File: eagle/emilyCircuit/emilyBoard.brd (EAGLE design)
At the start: 73.3 x 47 mm, 12 parts

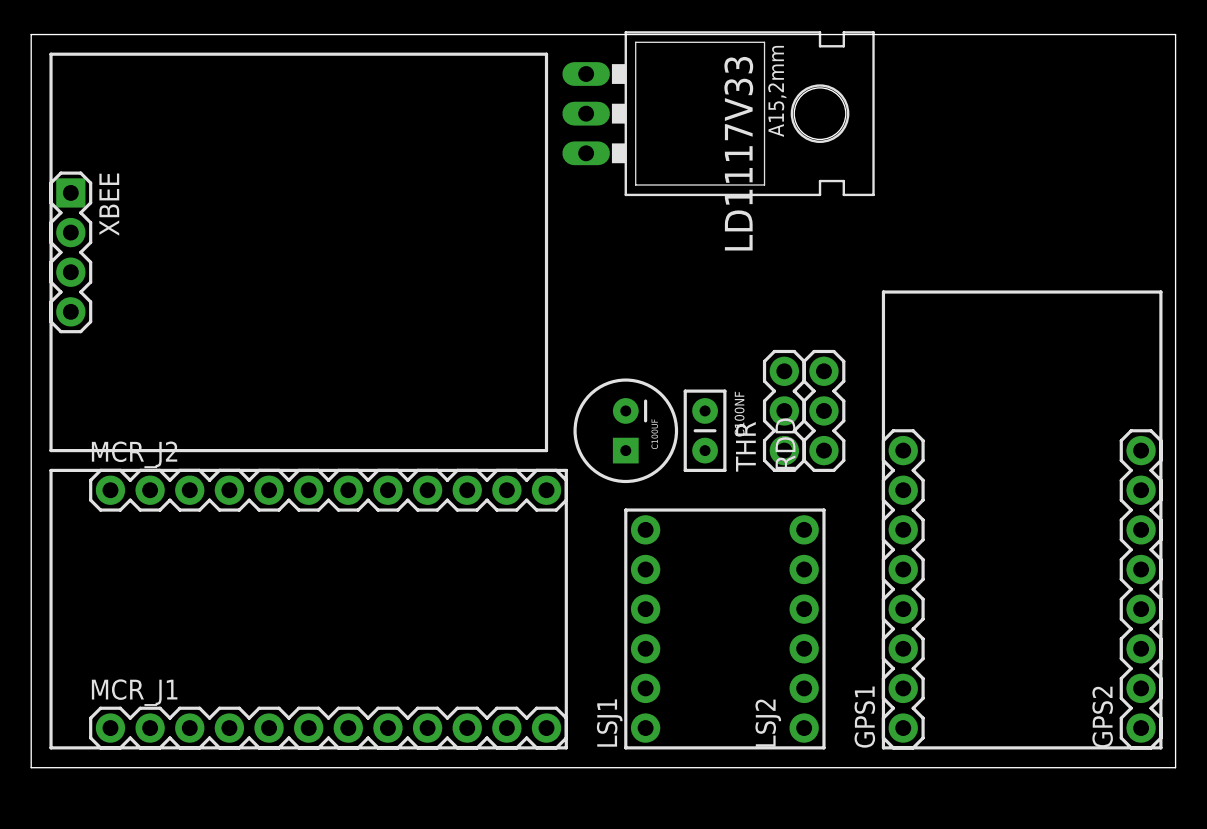
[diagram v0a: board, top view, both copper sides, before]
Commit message: Added connections to emily board
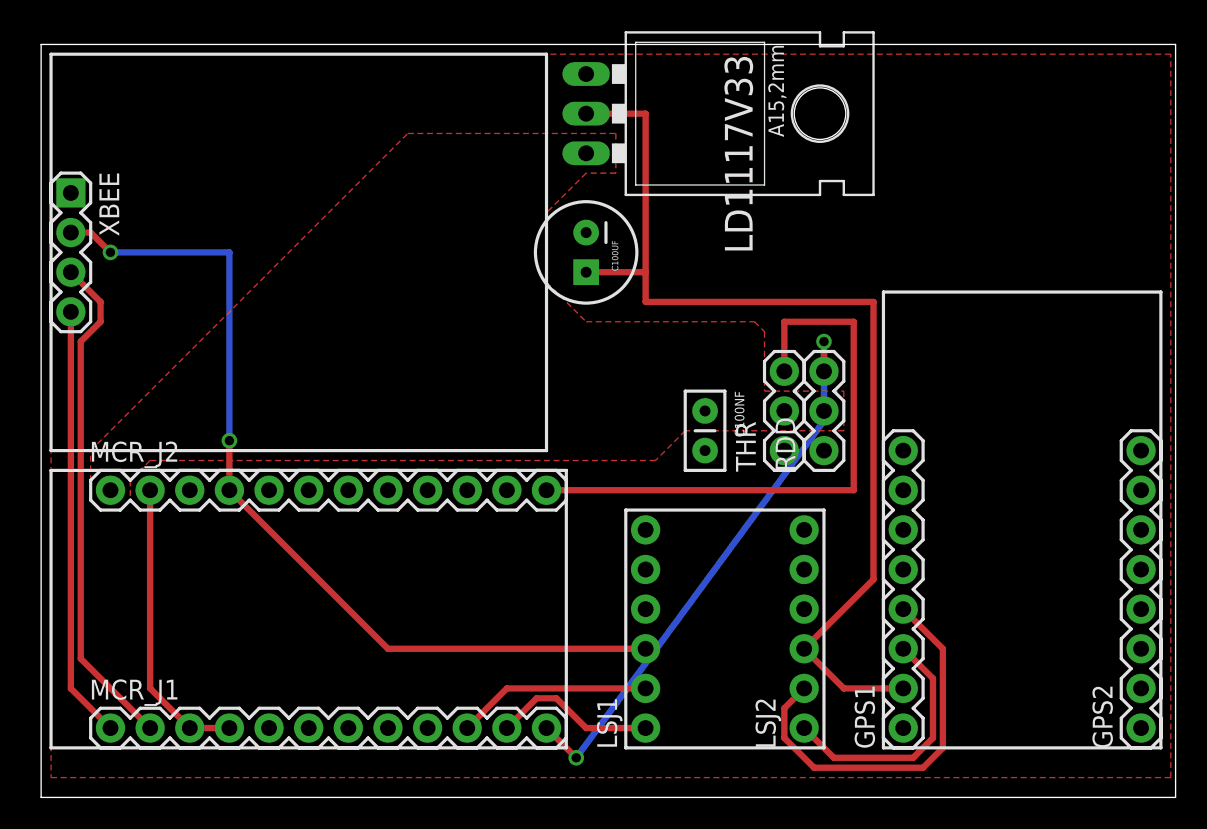
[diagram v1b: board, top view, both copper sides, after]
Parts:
- moved C100UF 11.7 mm to (54.6, 35.6)
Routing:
- net V3V3: track 0.00 -> 65.8 mm
- net VCC: track 0.00 -> 56.8 mm, vias 0 -> 2
- net TS: track 0.00 -> 38.1 mm
- net RS: track 0.00 -> 36.5 mm, vias 0 -> 2
- net RX1: track 0.00 -> 32.4 mm
- net TX1: track 0.00 -> 27.7 mm
- net RXG: track 0.00 -> 25.1 mm
- net GND: track 0.00 -> 18.8 mm
- net TXG: track 0.00 -> 16.1 mm
- net TX2: track 0.00 -> 12.5 mm
- net RX2: track 0.00 -> 10.5 mm
- added copper zone on layer 1, net GND
- added copper zone on layer 1, net VIN
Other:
- board size 73.3 x 47 mm -> 72.7 x 48.2 mm

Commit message: Updated EMILY PCB files with labels. Complies with OSHPark DRGs and Eagle ERGs.
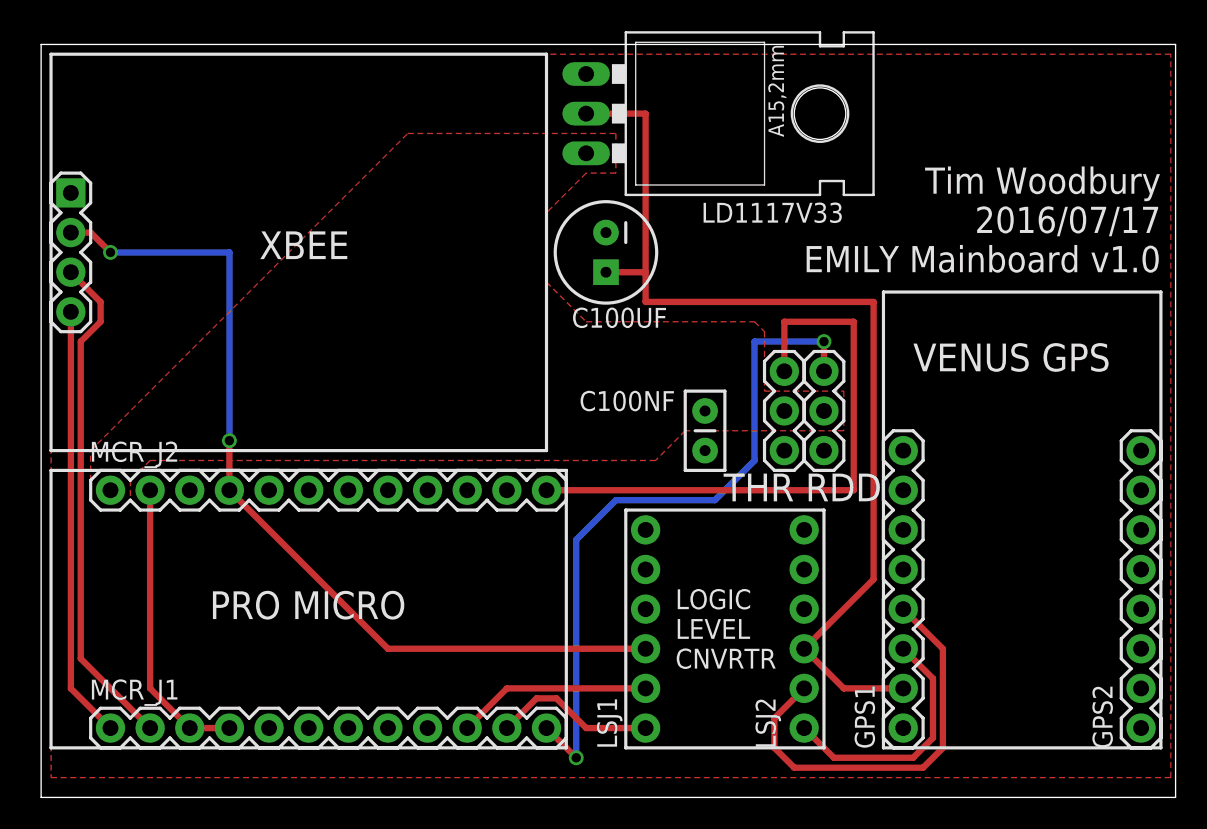
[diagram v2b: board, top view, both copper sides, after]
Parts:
- moved C100UF 1.27 mm to (55.9, 35.6)
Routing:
- net RS: track 36.5 -> 44.2 mm
- net RXG: track 25.1 -> 26.4 mm
- net V3V3: track 65.8 -> 64.5 mm
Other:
- board text added: "LOGIC LEVEL CNVRTR"
- board text added: "PRO MICRO"
- board text added: "Tim Woodbury 2016/07/17 EMILY Mainboard v1.0"
- board text added: "VENUS GPS"
